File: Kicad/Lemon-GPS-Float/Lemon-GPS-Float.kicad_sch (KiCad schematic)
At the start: 16 parts, among them J1 Micro_JST_01x02_Pin, J2 Micro_JST_01x02_Socket, J3 Micro_JST_01x02_Pin, J4 Micro_JST_01x02_Socket, SW1 SW_DPST

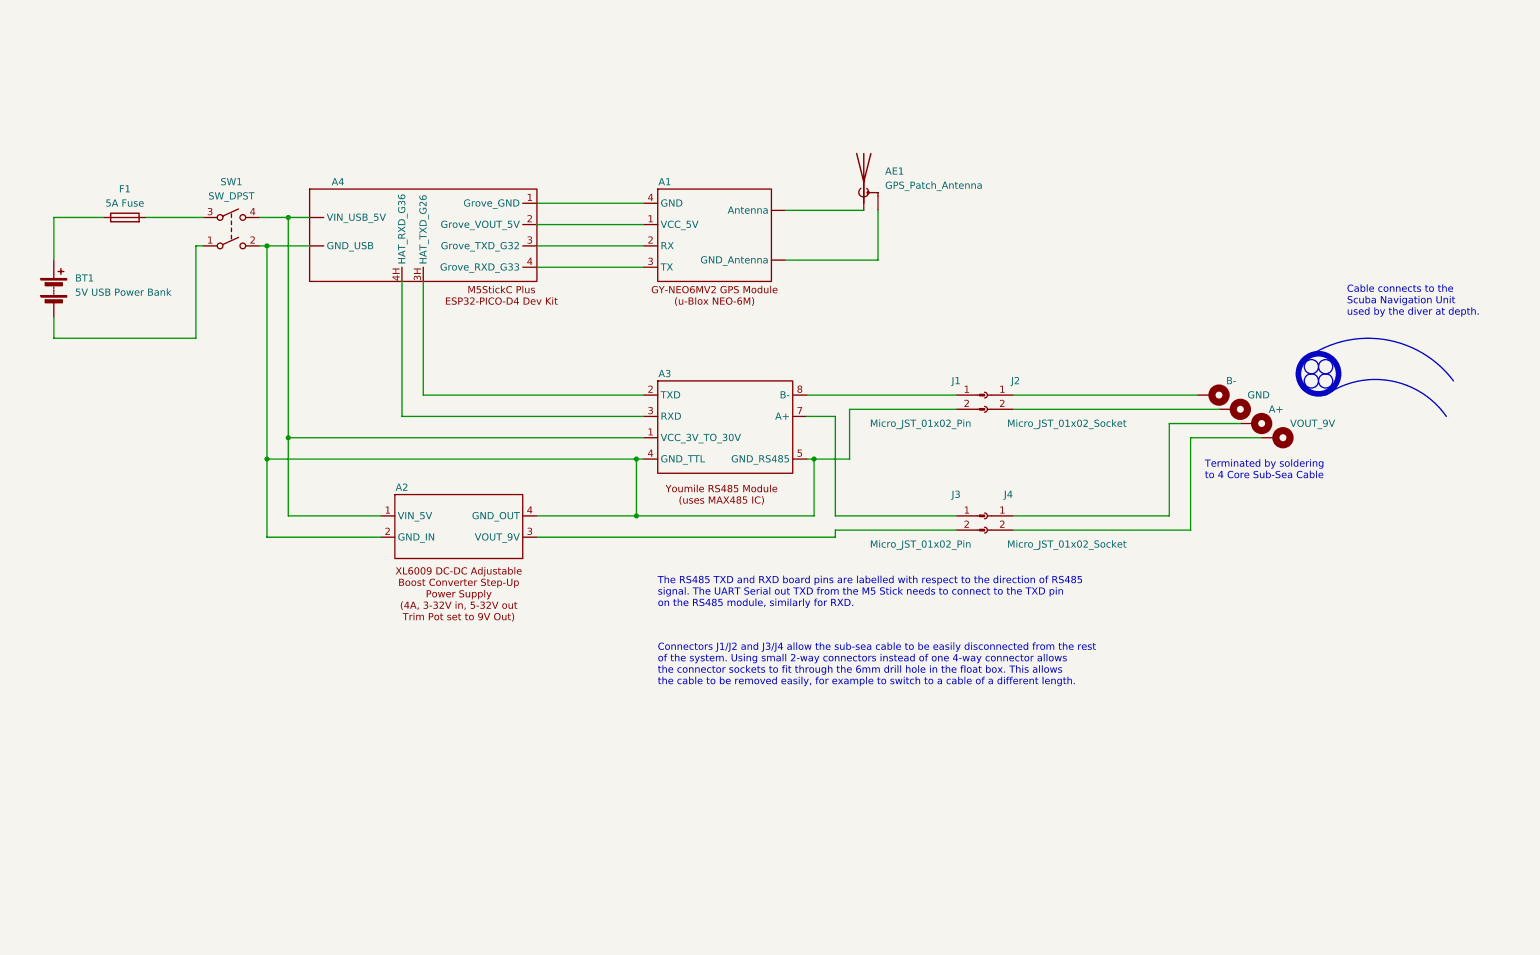
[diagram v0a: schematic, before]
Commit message: Added Audio Pod 1 and updated with images and tweaks other schematics.
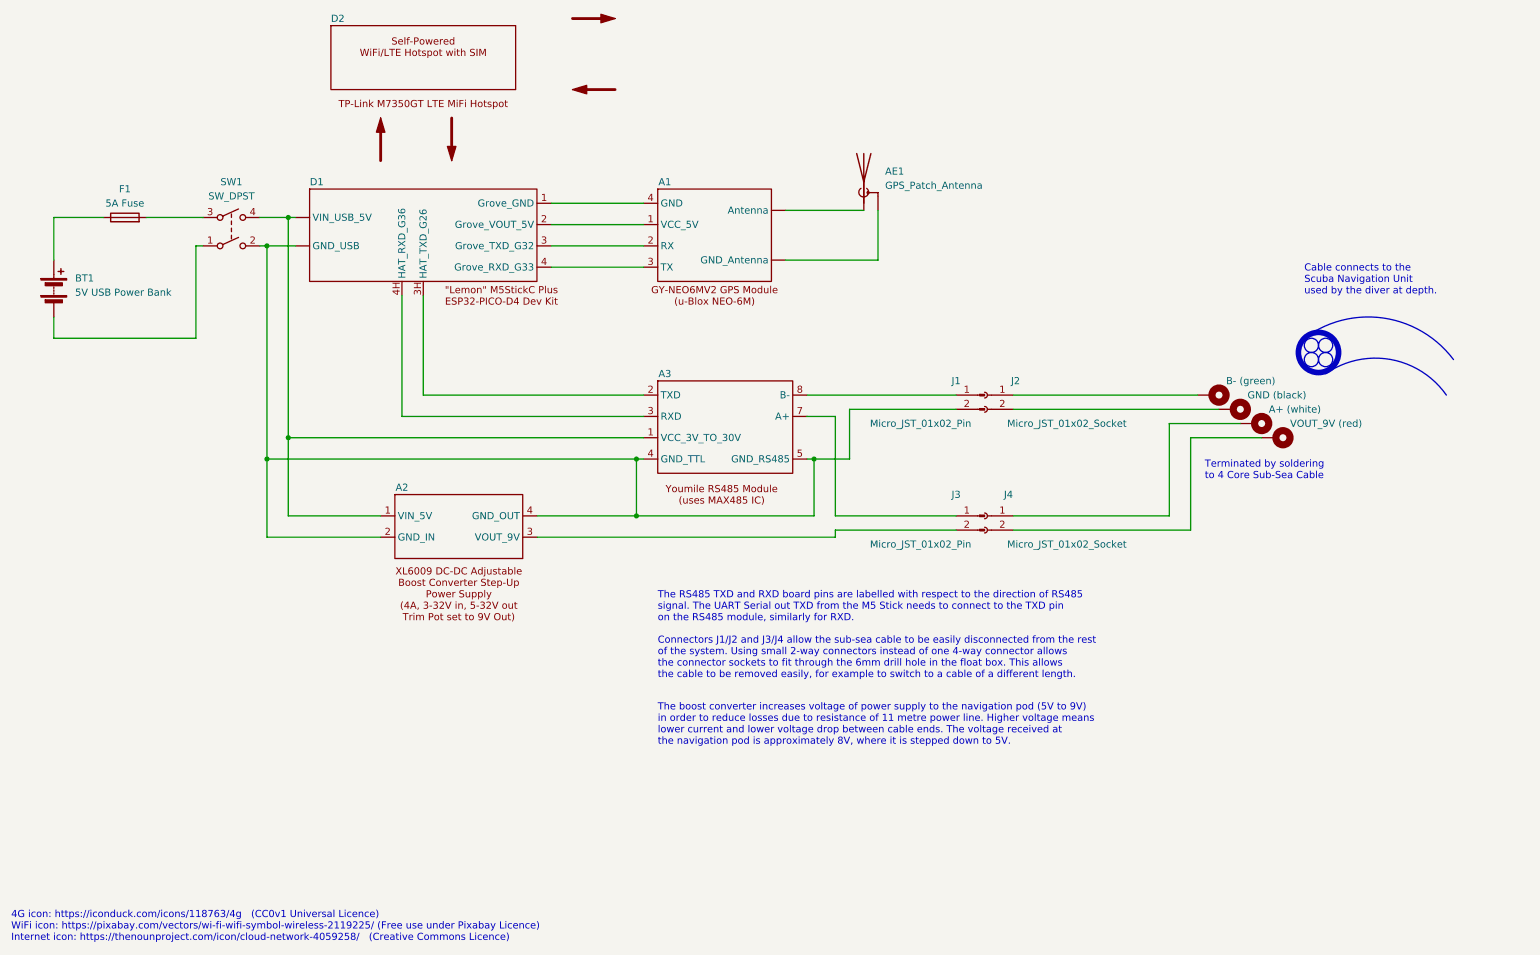
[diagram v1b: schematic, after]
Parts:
- added D2: ~, symbol Lemon-GPS-Float-Library:TP-Link_M7350_GT_LTE_MiFi
- H1: value B- -> B- (green)
- H2: value GND -> GND (black)
- H3: value A+ -> A+ (white)
- H4: value VOUT_9V -> VOUT_9V (red)
- renumbered A4 to D1
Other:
- note added: "4G icon: https://iconduck.com/icons/118763/4g (CC0v1 Universal Licence) WiFi icon: https://pixabay.com/vectors/wi-fi-wifi-symbol-wireless-2119225/ (Free use under Pixabay Licence) Internet icon: https://thenounproject.com/icon/cloud-network-4059258/ (Creative Commons Licence)"
- note added: "The boost converter increases voltage of power supply to the navigation pod (5V to 9V) in order to reduce losses due to resistance of 11 metre power line. Higher voltage means lower current and lower voltage drop between cable ends. The voltage received at the navigation pod is approximately 8V, where it is stepped down to 5V."
- title: (none) -> Mercator Origins GPS Float
- moved on the sheet: D1

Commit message: Added 2 x 1 K Ohm biasing resistors to RS485 output and added STL files
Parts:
- added R1, R2: 1KΩ, symbol Device:R_US
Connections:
- net at A2.1 (VIN_5V), A3.1 (VCC_3V_TO_30V), D1. (VIN_USB_5V)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: now also R1.1
- net at A2.2 (GND_IN), A2.4 (GND_OUT), A3.4 (GND_TTL)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: now also R2.1
- net at A3.7 (A+), J3.1 (Pin_1): now also R1.2
- net at A3.8 (B-), J1.1 (Pin_1): now also R2.2
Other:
- note added: "R1 and R2 are RS485 biasing resistors which provide a reference voltage when neither RS485 module is transmitting."
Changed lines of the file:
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@@
   (junction (at 60.96 69.85) (diameter 0) (color 0 0 0 0)
   )
+  (junction (at 162.56 100.33) (diameter 0) (color 0 0 0 0)
+  )
   (junction (at 127 118.11) (diameter 0) (color 0 0 0 0)
   )
   (junction (at 64.77 104.14) (diameter 0) (color 0 0 0 0)
   )
+  (junction (at 60.96 85.09) (diameter 0) (color 0 0 0 0)
+  )
+  (junction (at 64.77 81.28) (diameter 0) (color 0 0 0 0)
+  )
+  (junction (at 158.75 96.52) (diameter 0) (color 0 0 0 0)
+  )
+  (wire (pts (xy 158.75 96.52) (xy 184.15 96.52))
+    (stroke (width 0) (type default))
+  )
   (wire (pts (xy 153.67 72.39) (xy 170.18 72.39))
     (stroke (width 0) (type default))
@@
     (stroke (width 0) (type default))
   )
-  (wire (pts (xy 60.96 69.85) (xy 60.96 107.95))
+  (wire (pts (xy 60.96 69.85) (xy 60.96 85.09))
+    (stroke (width 0) (type default))
+  )
+  (wire (pts (xy 60.96 85.09) (xy 60.96 107.95))
     (stroke (width 0) (type default))
   )
@@
     (stroke (width 0) (type default))
   )
+  (wire (pts (xy 60.96 85.09) (xy 158.75 85.09))
+    (stroke (width 0) (type default))
+  )
   (wire (pts (xy 85.09 100.33) (xy 128.27 100.33))
     (stroke (width 0) (type default))
@@
     (stroke (width 0) (type default))
   )
+  (wire (pts (xy 162.56 88.9) (xy 162.56 100.33))
+    (stroke (width 0) (type default))
+  )
   (wire (pts (xy 59.69 64.77) (xy 64.77 64.77))
     (stroke (width 0) (type default))
@@
     (stroke (width 0) (type default))
   )
-  (wire (pts (xy 64.77 64.77) (xy 64.77 104.14))
+  (wire (pts (xy 64.77 64.77) (xy 64.77 81.28))
+    (stroke (width 0) (type default))
+  )
+  (wire (pts (xy 158.75 92.71) (xy 158.75 96.52))
     (stroke (width 0) (type default))
   )
@@
     (stroke (width 0) (type default))
   )
-  (wire (pts (xy 157.48 96.52) (xy 184.15 96.52))
-    (stroke (width 0) (type default))
-  )
   (wire (pts (xy 85.09 78.74) (xy 85.09 100.33))
     (stroke (width 0) (type default))
@@
     (stroke (width 0) (type default))
   )
+  (wire (pts (xy 157.48 96.52) (xy 158.75 96.52))
+    (stroke (width 0) (type default))
+  )
+  (wire (pts (xy 64.77 81.28) (xy 64.77 104.14))
+    (stroke (width 0) (type default))
+  )
   (wire (pts (xy 22.86 82.55) (xy 22.86 86.36))
     (stroke (width 0) (type default))
@@
   )
   (wire (pts (xy 222.25 118.11) (xy 222.25 101.6))
+    (stroke (width 0) (type default))
+  )
+  (wire (pts (xy 64.77 81.28) (xy 162.56 81.28))
     (stroke (width 0) (type default))
   )
@@
   )
   (text "The boost converter increases voltage of power supply to the navigation pod (5V to 9V)\nin order to reduce losses due to resistance of 11 metre power line. Higher voltage means\nlower current and lower voltage drop between cable ends. The voltage received at\nthe navigation pod is approximately 8V, where it is stepped down to 5V.\n\n"
-    (at 130.81 161.29 0)
+    (at 130.81 157.48 0)
     (effects (font (size 1.27 1.27)) (justify left bottom))
   )
@@
   )
   (text "The RS485 TXD and RXD board pins are labelled with respect to the direction of RS485 \nsignal. The UART Serial out TXD from the M5 Stick needs to connect to the TXD pin\non the RS485 module, similarly for RXD."
-    (at 130.81 137.16 0)
+    (at 130.81 134.62 0)
     (effects (font (size 1.27 1.27)) (justify left bottom))
   )
@@
     (effects (font (size 1.27 1.27)) (justify left bottom))
   )
+  (text "R1 and R2 are RS485 biasing resistors which provide a reference voltage when neither \nRS485 module is transmitting."
+    (at 130.81 161.29 0)
+    (effects (font (size 1.27 1.27)) (justify left bottom))
+  )
   (text "Connectors J1/J2 and J3/J4 allow the sub-sea cable to be easily disconnected from the rest\nof the system. Using small 2-way connectors instead of one 4-way connector allows\nthe connector sockets to fit through the 6mm drill hole in the float box. This allows\nthe cable to be removed easily, for example to switch to a cable of a different length."
-    (at 130.81 147.32 0)
+    (at 130.81 144.78 0)
     (effects (font (size 1.27 1.27)) (justify left bottom))
   )
@@
         (path "/31bb21f9-9995-4db5-8ef0-b85c32a3cdf6"
           (reference "H4") (unit 1)
+        )
+      )
+    )
+  )
+  (symbol (lib_id "Device:R_US") (at 162.56 85.09 0) (unit 1)
+    (in_bom yes) (on_board yes) (dnp no) (fields_autoplaced)
+    (property "Reference" "R1" (at 165.1 83.82 0)
+      (effects (font (size 1.27 1.27)) (justify left))
+    )
+    (property "Value" "1KΩ" (at 165.1 86.36 0)
+      (effects (font (size 1.27 1.27)) (justify left))
+    )
+    (property "Footprint" "" (at 163.576 85.344 90)
+      (effects (font (size 1.27 1.27)) hide)
+    )
+    (property "Datasheet" "~" (at 162.56 85.09 0)
+      (effects (font (size 1.27 1.27)) hide)
+    )
+    (pin "1")
+    (pin "2")
+    (instances
+      (project "Lemon-GPS-Float"
+        (path "/31bb21f9-9995-4db5-8ef0-b85c32a3cdf6"
+          (reference "R1") (unit 1)
         )
       )
@@
         )
       )
+    )
+  )
+  (symbol (lib_id "Device:R_US") (at 158.75 88.9 0) (unit 1)
+    (in_bom yes) (on_board yes) (dnp no)
+    (property "Reference" "R2" (at 153.67 87.63 0)
+      (effects (font (size 1.27 1.27)) (justify left))
+    )
+    (property "Value" "1KΩ" (at 152.4 90.17 0)
+      (effects (font (size 1.27 1.27)) (justify left))
+    )
+    (property "Footprint" "" (at 159.766 89.154 90)
+      (effects (font (size 1.27 1.27)) hide)
+    )
+    (property "Datasheet" "~" (at 158.75 88.9 0)
+      (effects (font (size 1.27 1.27)) hide)
+    )
+    (pin "1")
+    (pin "2")
+    (instances
+      (project "Lemon-GPS-Float"
+        (path "/31bb21f9-9995-4db5-8ef0-b85c32a3cdf6"
+          (reference "R2") (unit 1)
+        )
+      )
